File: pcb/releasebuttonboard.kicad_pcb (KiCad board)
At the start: 2 copper layers, 65 x 56 mm, 30 parts, among them SW1 ROTENC, U1 24C16, U2 RASPIPLUSHEADER, U3 OLEDHeader, U4 REncHeader, U5 BtnHeader, U6 PAM8407, U7 REncHeader

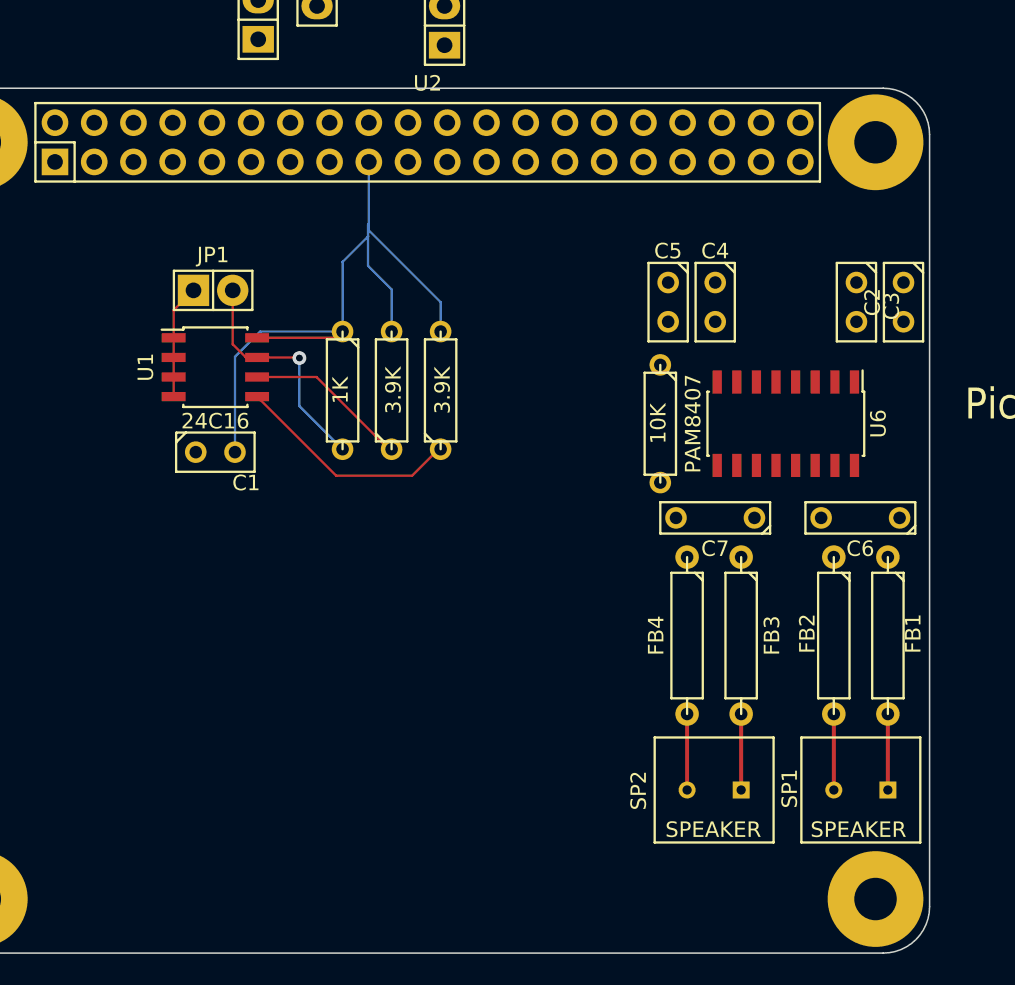
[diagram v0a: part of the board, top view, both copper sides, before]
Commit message: Track routing for the audio portion of the PCB.
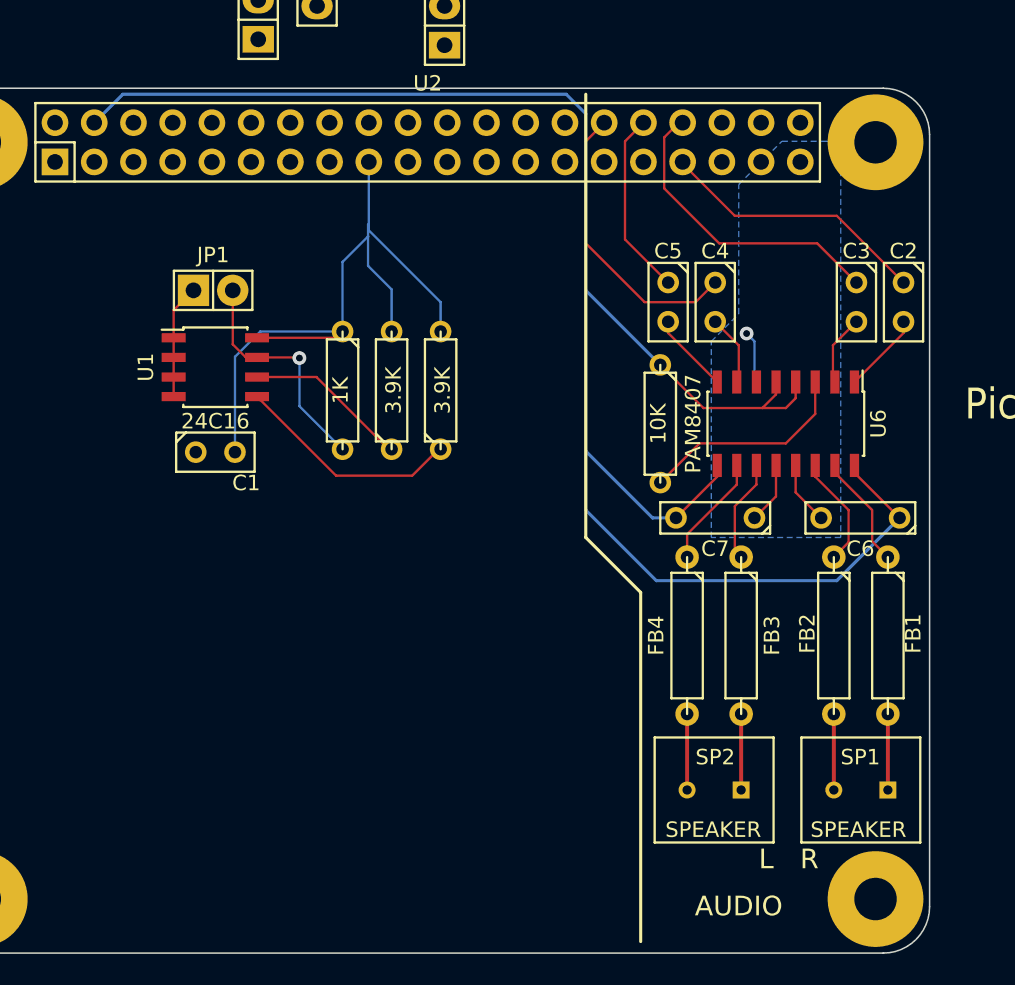
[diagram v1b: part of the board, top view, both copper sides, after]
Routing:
- net AVCC: track 0.39 -> 119.9 mm
- net GND: track 7.41 -> 54.2 mm
- net /AUD_R: track 0.00 -> 17.6 mm
- net Net-(R4-Pad2): track 0.00 -> 13.9 mm
- net /AUD_L: track 0.01 -> 12.5 mm
- net Net-(FB1-Pad1): track 0.00 -> 7.36 mm
- net Net-(FB4-Pad1): track 0.08 -> 7.35 mm
- net Net-(FB2-Pad1): track 0.00 -> 7.23 mm
- net Net-(FB3-Pad1): track 0.42 -> 7.10 mm
- net Net-(C5-Pad2): track 0.00 -> 5.22 mm
- net Net-(C2-Pad2): track 0.00 -> 5.22 mm
- net Net-(C4-Pad2): track 0.00 -> 4.59 mm
- net Net-(C3-Pad2): track 0.00 -> 4.59 mm
- net (no net): track 0.00 -> 3.51 mm, vias 0 -> 1
- added copper zone on B.Cu, net GND
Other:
- board text added: "AUDIO"
- board text added: "L"
- board text added: "R"

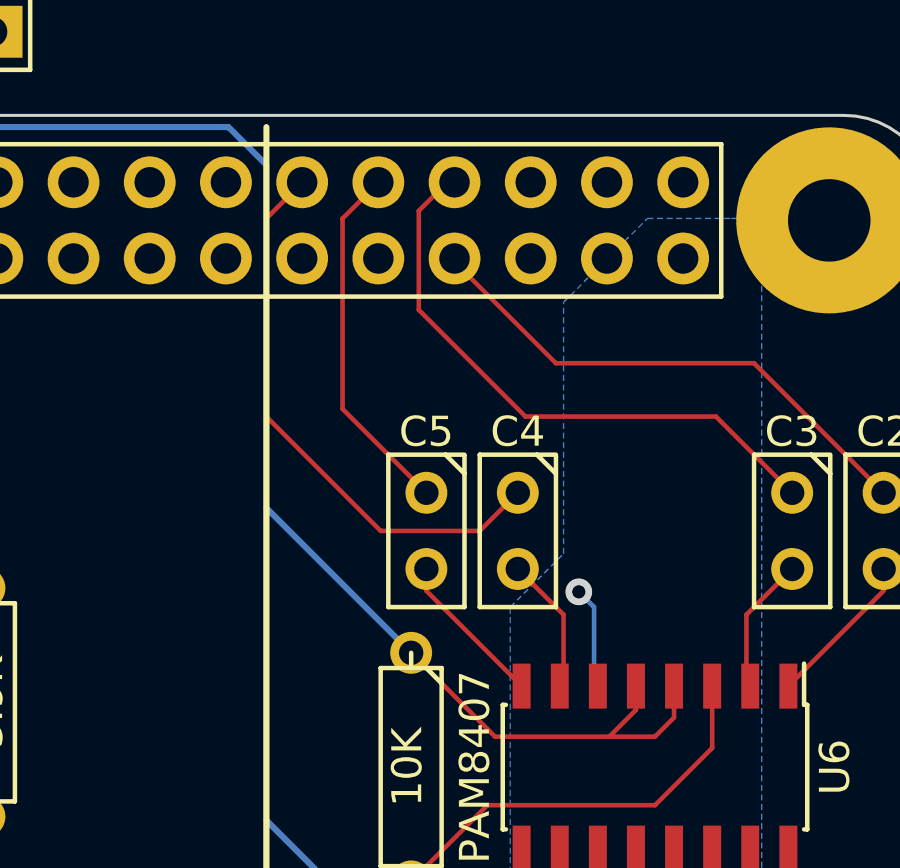
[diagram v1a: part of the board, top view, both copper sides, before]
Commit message: Add dummy copper layer to fake out signal connections on header pin.
In order for the DRC to consider the routing to be complete it needs to
know that the GND, VCC and AVCC pins (respectively) on the Raspberry Pi
header will be connected by the Pi board itself and thus don't need to
actually be connected on this board. We achieve this by providing a dummy
copper layer that won't be included in the fab order.
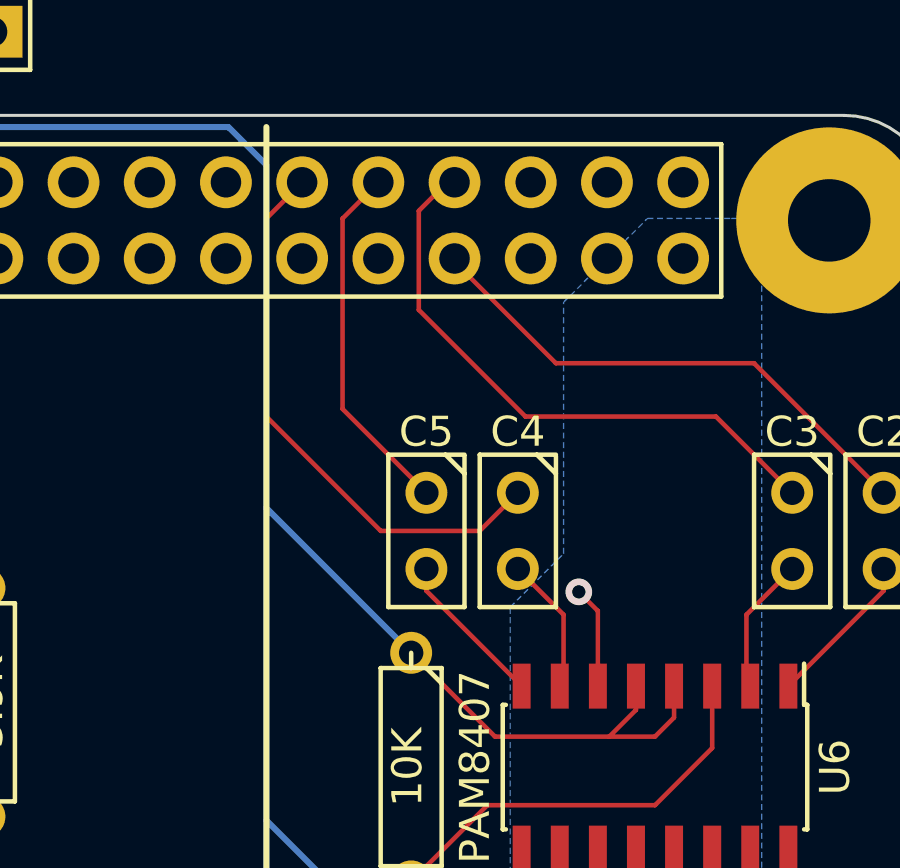
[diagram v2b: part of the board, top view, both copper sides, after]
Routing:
- net GND: track 54.2 -> 112.9 mm, vias 0 -> 1
- net VCC: track 47.4 -> 69.1 mm
- net (no net): track 3.51 -> 0.00 mm, vias 1 -> 0
- net AVCC: track 119.9 -> 122.4 mm
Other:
- copper layers 2 -> 4
- board text added: "This dummy layer is here only to trick DRC into considering the GND and Supply pins on the Pi header to be electrically connected. It should not be included when manufacturing. This is just a two-layer design."
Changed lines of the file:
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@@
   (general
     (links 76)
-    (no_connects 35)
+    (no_connects 25)
     (area 95.449999 67.949999 160.550001 124.050001)
     (thickness 1.6)
-    (drawings 16)
-    (tracks 132)
+    (drawings 17)
+    (tracks 158)
     (zones 0)
     (modules 30)
@@
   (page A4)
   (layers
-    (0 F.Cu signal)
-    (31 B.Cu signal)
+    (0 F.Cu mixed)
+    (1 In1.Cu mixed hide)
+    (2 In2.Cu mixed hide)
+    (31 B.Cu mixed)
     (32 B.Adhes user)
     (33 F.Adhes user)
@@
     (pad 1 thru_hole circle (at 0 0) (size 6.2 6.2) (drill 2.75) (layers *.Cu *.Mask F.SilkS))
   )
+  (gr_text "This dummy layer is here only to trick DRC into\nconsidering the GND and Supply pins on the\nPi header to be electrically connected.\n\nIt should not be included when manufacturing.\nThis is just a two-layer design.\n" (at 103.694 120.204) (layer In1.Cu)
+    (effects (font (size 0.508 0.508) (thickness 0.127)) (justify left))
+  )
   (gr_text AUDIO (at 148.144 120.966) (layer F.SilkS)
     (effects (font (thickness 0.1905)))
@@
   (gr_line (start 95.5 71) (end 95.5 121) (angle 90) (layer Edge.Cuts) (width 0.1))
   (gr_arc (start 98.5 71) (end 95.5 71) (angle 90) (layer Edge.Cuts) (width 0.1))
-  (segment (start 149.16 86.93) (end 149.16 84.39) (width 0.1524) (layer B.Cu) (net 0))
-  (segment (start 148.652 83.882) (end 148.652 83.628) (width 0.1524) (layer F.Cu) (net 0))
-  (via (at 148.652 83.882) (size 0.889) (layers F.Cu B.Cu) (net 0))
-  (segment (start 149.16 84.39) (end 148.652 83.882) (width 0.1524) (layer B.Cu) (net 0))
+  (segment (start 149.287 87.024) (end 149.287 84.517) (width 0.1524) (layer F.Cu) (net 1) (status 400000))
+  (via (at 148.652 83.882) (size 0.889) (layers F.Cu B.Cu) (net 1))
+  (segment (start 149.287 84.517) (end 148.652 83.882) (width 0.1524) (layer F.Cu) (net 1))
+  (segment (start 126.73 70.23) (end 126.73 70.244) (width 0.1524) (layer In1.Cu) (net 1) (status C00000))
+  (segment (start 126.73 70.244) (end 125.538 71.436) (width 0.1524) (layer In1.Cu) (net 1) (status 400000))
+  (segment (start 152.13 72.77) (end 152.13 72.628) (width 0.1524) (layer In1.Cu) (net 1) (status C00000))
+  (segment (start 152.13 72.628) (end 150.938 71.436) (width 0.1524) (layer In1.Cu) (net 1) (status 400000))
+  (segment (start 150.938 71.436) (end 143.572 71.436) (width 0.1524) (layer In1.Cu) (net 1))
+  (segment (start 144.51 70.23) (end 144.51 70.498) (width 0.1524) (layer In1.Cu) (net 1) (status C00000))
+  (segment (start 144.51 70.498) (end 143.572 71.436) (width 0.1524) (layer In1.Cu) (net 1) (status 400000))
+  (segment (start 143.572 71.436) (end 138.238 71.436) (width 0.1524) (layer In1.Cu) (net 1))
+  (segment (start 139.43 70.23) (end 139.43 70.244) (width 0.1524) (layer In1.Cu) (net 1) (status C00000))
+  (segment (start 139.43 70.244) (end 138.238 71.436) (width 0.1524) (layer In1.Cu) (net 1) (status 400000))
+  (segment (start 138.238 71.436) (end 132.65 71.436) (width 0.1524) (layer In1.Cu) (net 1))
+  (segment (start 117.918 71.436) (end 125.538 71.436) (width 0.1524) (layer In1.Cu) (net 1))
+  (segment (start 125.538 71.436) (end 132.65 71.436) (width 0.1524) (layer In1.Cu) (net 1))
+  (segment (start 132.65 71.436) (end 133.016 71.436) (width 0.1524) (layer In1.Cu) (net 1))
+  (segment (start 133.016 71.436) (end 134.35 72.77) (width 0.1524) (layer In1.Cu) (net 1) (status 800000))
+  (segment (start 119.11 70.23) (end 119.11 70.244) (width 0.1524) (layer In1.Cu) (net 1) (status C00000))
+  (segment (start 119.11 70.244) (end 117.918 71.436) (width 0.1524) (layer In1.Cu) (net 1) (status 400000))
+  (segment (start 117.918 71.436) (end 112.584 71.436) (width 0.1524) (layer In1.Cu) (net 1))
+  (segment (start 108.95 70.23) (end 108.95 70.342) (width 0.1524) (layer In1.Cu) (net 1) (status C00000))
+  (segment (start 108.95 70.342) (end 110.044 71.436) (width 0.1524) (layer In1.Cu) (net 1) (status 400000))
+  (segment (start 110.044 71.436) (end 112.584 71.436) (width 0.1524) (layer In1.Cu) (net 1))
+  (segment (start 112.584 71.436) (end 112.696 71.436) (width 0.1524) (layer In1.Cu) (net 1))
+  (segment (start 112.696 71.436) (end 114.03 72.77) (width 0.1524) (layer In1.Cu) (net 1) (status 800000))
   (segment (start 144.51 70.23) (end 144.27 70.23) (width 0.1524) (layer F.Cu) (net 1))
   (segment (start 144.27 70.23) (end 143.318 71.182) (width 0.1524) (layer F.Cu) (net 1))
@@
   (segment (start 146.874 78.04) (end 153.224 78.04) (width 0.1524) (layer F.Cu) (net 1))
   (segment (start 153.224 78.04) (end 155.764 80.58) (width 0.1524) (layer F.Cu) (net 1))
-  (segment (start 139.43 70.23) (end 139.43 70.244) (width 0.1524) (layer F.Cu) (net 1))
   (segment (start 139.43 70.244) (end 138.238 71.436) (width 0.1524) (layer F.Cu) (net 1))
   (segment (start 145.35 81.85) (end 146.62 80.58) (width 0.1524) (layer F.Cu) (net 1))
@@
   (segment (start 111.554 84.159) (end 111.554 82.372) (width 0.1524) (layer F.Cu) (net 1))
   (segment (start 111.554 82.372) (end 112.838 81.088) (width 0.1524) (layer F.Cu) (net 1))
+  (segment (start 103.87 72.77) (end 104.012 72.77) (width 0.1524) (layer In1.Cu) (net 2) (status C00000))
+  (segment (start 104.012 72.77) (end 105.726 74.484) (width 0.1524) (layer In1.Cu) (net 2) (status 400000))
+  (segment (start 105.726 74.484) (end 122.476 74.484) (width 0.1524) (layer In1.Cu) (net 2))
+  (segment (start 122.476 74.484) (end 124.19 72.77) (width 0.1524) (layer In1.Cu) (net 2) (status 800000))
   (segment (start 115.524 91.564) (end 115.524 85.387) (width 0.1524) (layer B.Cu) (net 2))
   (segment (start 117.156 83.755) (end 122.49 83.755) (width 0.1524) (layer B.Cu) (net 2))
@@
   (segment (start 151.192 90.994) (end 153.097 89.089) (width 0.1524) (layer F.Cu) (net 20))
   (segment (start 145.604 90.994) (end 151.192 90.994) (width 0.1524) (layer F.Cu) (net 20))
+  (segment (start 103.87 70.23) (end 106.41 70.23) (width 0.1524) (layer In1.Cu) (net 36) (status C00000))
   (segment (start 138.238 91.502) (end 138.238 95.312) (width 0.2032) (layer B.Cu) (net 36))
   (segment (start 154.494 99.884) (end 158.558 95.82) (width 0.2032) (layer B.Cu) (net 36))
